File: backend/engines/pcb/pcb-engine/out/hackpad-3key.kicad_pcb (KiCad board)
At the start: 2 copper layers, 58.3 x 43 mm, 8 parts, among them SW1 ESC, SW2 2, SW3 3, U1 XIAO RP2040

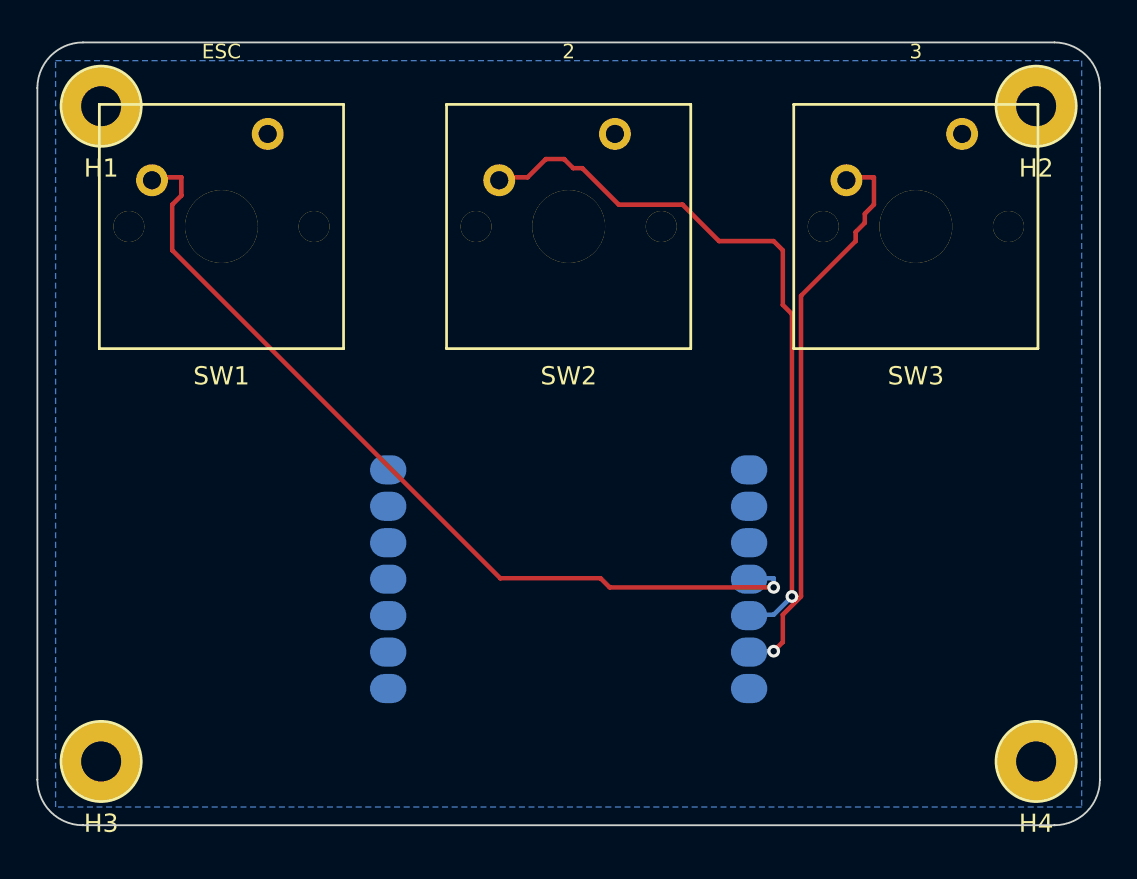
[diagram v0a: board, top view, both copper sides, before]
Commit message: case compiler: pcb result -> parametric openscad. xiao flipped 180 so usb faces the board edge. job #2 (ninepad) end to end with case artifacts. openscad-verified stls for all reference boards
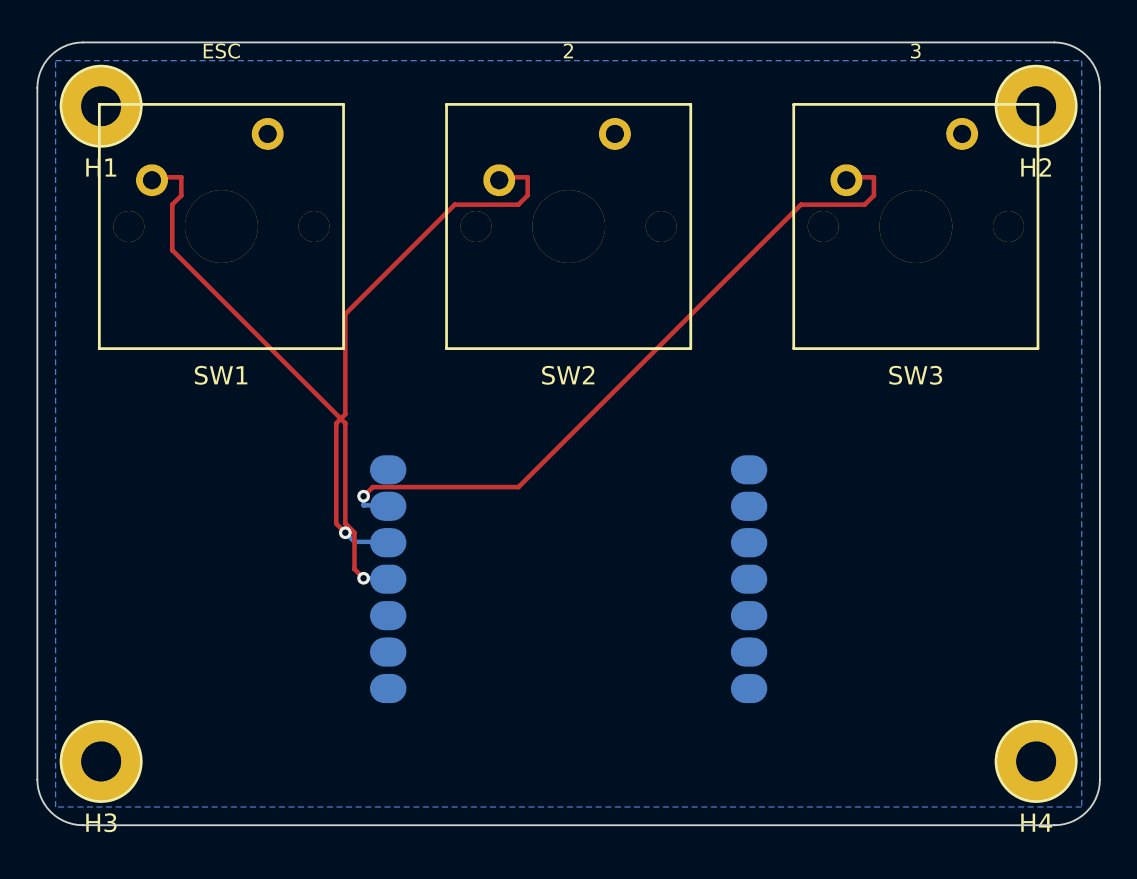
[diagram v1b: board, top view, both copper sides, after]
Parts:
- turned U1 to -180 degrees
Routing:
- net K1: track 48.4 -> 29.6 mm
- net K2: track 40.1 -> 30.3 mm
- net K3: track 31.3 -> 39.3 mm
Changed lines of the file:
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@@
   (pad "peg1" thru_hole circle (at -5.08 0) (size 1.7 1.7) (drill 1.7) (layers "*.Cu" "*.Mask") (remove_unused_layers) (keep_end_layers))
   (pad "peg2" thru_hole circle (at 5.08 0) (size 1.7 1.7) (drill 1.7) (layers "*.Cu" "*.Mask") (remove_unused_layers) (keep_end_layers)))
-(footprint "keeberia:Module_Seeed_XIAO" (layer B.Cu) (at 0 7.975000000000001)
+(footprint "keeberia:Module_Seeed_XIAO" (layer B.Cu) (at 0 7.975000000000001 -180)
   (attr smd)
   (fp_text reference "U1" (at 0 -9.95) (layer B.SilkS) (effects (font (size 1 1) (thickness 0.15))))
@@
   (fp_circle (center 0 0) (end 2.2 0) (stroke (width 0.15) (type solid)) (fill none) (layer F.SilkS))
   (pad "1" thru_hole circle (at 0 0) (size 4.4 4.4) (drill 2.2) (layers "*.Cu" "*.Mask") (remove_unused_layers) (keep_end_layers)))
+  (segment (start 15.25 -14.075) (end 16.75 -14.075) (width 0.25) (layer F.Cu) (net 5 "K3"))
+  (segment (start 16.75 -14.075) (end 16.75 -13.075) (width 0.25) (layer F.Cu) (net 5 "K3"))
+  (segment (start 16.75 -13.075) (end 16.25 -12.575) (width 0.25) (layer F.Cu) (net 5 "K3"))
+  (segment (start 16.25 -12.575) (end 12.75 -12.575) (width 0.25) (layer F.Cu) (net 5 "K3"))
+  (segment (start 12.75 -12.575) (end -2.75 2.925) (width 0.25) (layer F.Cu) (net 5 "K3"))
+  (segment (start -2.75 2.925) (end -10.75 2.925) (width 0.25) (layer F.Cu) (net 5 "K3"))
+  (segment (start -10.75 2.925) (end -11.25 3.425) (width 0.25) (layer F.Cu) (net 5 "K3"))
+  (segment (start -11.25 3.425) (end -11.25 3.925) (width 0.25) (layer B.Cu) (net 5 "K3"))
+  (segment (start -11.25 3.925) (end -9.75 3.925) (width 0.25) (layer B.Cu) (net 5 "K3"))
   (segment (start -22.75 -14.075) (end -21.25 -14.075) (width 0.25) (layer F.Cu) (net 3 "K1"))
   (segment (start -21.25 -14.075) (end -21.25 -13.075) (width 0.25) (layer F.Cu) (net 3 "K1"))
   (segment (start -21.25 -13.075) (end -21.75 -12.575) (width 0.25) (layer F.Cu) (net 3 "K1"))
   (segment (start -21.75 -12.575) (end -21.75 -10.075) (width 0.25) (layer F.Cu) (net 3 "K1"))
-  (segment (start -21.75 -10.075) (end -3.75 7.925) (width 0.25) (layer F.Cu) (net 3 "K1"))
-  (segment (start -3.75 7.925) (end 1.75 7.925) (width 0.25) (layer F.Cu) (net 3 "K1"))
-  (segment (start 1.75 7.925) (end 2.25 8.425) (width 0.25) (layer F.Cu) (net 3 "K1"))
-  (segment (start 2.25 8.425) (end 11.25 8.425) (width 0.25) (layer F.Cu) (net 3 "K1"))
-  (segment (start 11.25 8.425) (end 11.25 7.925) (width 0.25) (layer B.Cu) (net 3 "K1"))
-  (segment (start 11.25 7.925) (end 9.75 7.925) (width 0.25) (layer B.Cu) (net 3 "K1"))
+  (segment (start -21.75 -10.075) (end -12.25 -0.575) (width 0.25) (layer F.Cu) (net 3 "K1"))
+  (segment (start -12.25 -0.575) (end -12.25 4.925) (width 0.25) (layer F.Cu) (net 3 "K1"))
+  (segment (start -12.25 4.925) (end -11.75 5.425) (width 0.25) (layer F.Cu) (net 3 "K1"))
+  (segment (start -11.75 5.425) (end -11.75 7.425) (width 0.25) (layer F.Cu) (net 3 "K1"))
+  (segment (start -11.75 7.425) (end -11.25 7.925) (width 0.25) (layer F.Cu) (net 3 "K1"))
+  (segment (start -11.25 7.925) (end -9.75 7.925) (width 0.25) (layer B.Cu) (net 3 "K1"))
   (segment (start -3.75 -14.075) (end -2.25 -14.075) (width 0.25) (layer F.Cu) (net 4 "K2"))
-  (segment (start -2.25 -14.075) (end -1.25 -15.075) (width 0.25) (layer F.Cu) (net 4 "K2"))
-  (segment (start -1.25 -15.075) (end -0.25 -15.075) (width 0.25) (layer F.Cu) (net 4 "K2"))
-  (segment (start -0.25 -15.075) (end 0.25 -14.575) (width 0.25) (layer F.Cu) (net 4 "K2"))
-  (segment (start 0.25 -14.575) (end 0.75 -14.575) (width 0.25) (layer F.Cu) (net 4 "K2"))
-  (segment (start 0.75 -14.575) (end 2.75 -12.575) (width 0.25) (layer F.Cu) (net 4 "K2"))
-  (segment (start 2.75 -12.575) (end 6.25 -12.575) (width 0.25) (layer F.Cu) (net 4 "K2"))
-  (segment (start 6.25 -12.575) (end 8.25 -10.575) (width 0.25) (layer F.Cu) (net 4 "K2"))
-  (segment (start 8.25 -10.575) (end 11.25 -10.575) (width 0.25) (layer F.Cu) (net 4 "K2"))
-  (segment (start 11.25 -10.575) (end 11.75 -10.075) (width 0.25) (layer F.Cu) (net 4 "K2"))
-  (segment (start 11.75 -10.075) (end 11.75 -7.075) (width 0.25) (layer F.Cu) (net 4 "K2"))
-  (segment (start 11.75 -7.075) (end 12.25 -6.575) (width 0.25) (layer F.Cu) (net 4 "K2"))
-  (segment (start 12.25 -6.575) (end 12.25 8.925) (width 0.25) (layer F.Cu) (net 4 "K2"))
-  (segment (start 12.25 8.925) (end 11.25 9.925) (width 0.25) (layer B.Cu) (net 4 "K2"))
-  (segment (start 11.25 9.925) (end 9.75 9.925) (width 0.25) (layer B.Cu) (net 4 "K2"))
-  (segment (start 15.25 -14.075) (end 16.75 -14.075) (width 0.25) (layer F.Cu) (net 5 "K3"))
-  (segment (start 16.75 -14.075) (end 16.75 -12.575) (width 0.25) (layer F.Cu) (net 5 "K3"))
-  (segment (start 16.75 -12.575) (end 16.25 -12.075) (width 0.25) (layer F.Cu) (net 5 "K3"))
-  (segment (start 16.25 -12.075) (end 16.25 -11.575) (width 0.25) (layer F.Cu) (net 5 "K3"))
-  (segment (start 16.25 -11.575) (end 15.75 -11.075) (width 0.25) (layer F.Cu) (net 5 "K3"))
-  (segment (start 15.75 -11.075) (end 15.75 -10.575) (width 0.25) (layer F.Cu) (net 5 "K3"))
-  (segment (start 15.75 -10.575) (end 12.75 -7.575) (width 0.25) (layer F.Cu) (net 5 "K3"))
-  (segment (start 12.75 -7.575) (end 12.75 8.925) (width 0.25) (layer F.Cu) (net 5 "K3"))
-  (segment (start 12.75 8.925) (end 11.75 9.925) (width 0.25) (layer F.Cu) (net 5 "K3"))
-  (segment (start 11.75 9.925) (end 11.75 11.425) (width 0.25) (layer F.Cu) (net 5 "K3"))
-  (segment (start 11.75 11.425) (end 11.25 11.925) (width 0.25) (layer F.Cu) (net 5 "K3"))
-  (segment (start 11.25 11.925) (end 9.75 11.925) (width 0.25) (layer B.Cu) (net 5 "K3"))
-  (via (at 11.25 8.425) (size 0.7) (drill 0.35) (layers "F.Cu" "B.Cu") (net 3 "K1"))
-  (via (at 12.25 8.925) (size 0.7) (drill 0.35) (layers "F.Cu" "B.Cu") (net 4 "K2"))
-  (via (at 11.25 11.925) (size 0.7) (drill 0.35) (layers "F.Cu" "B.Cu") (net 5 "K3"))
+  (segment (start -2.25 -14.075) (end -2.25 -13.075) (width 0.25) (layer F.Cu) (net 4 "K2"))
+  (segment (start -2.25 -13.075) (end -2.75 -12.575) (width 0.25) (layer F.Cu) (net 4 "K2"))
+  (segment (start -2.75 -12.575) (end -6.25 -12.575) (width 0.25) (layer F.Cu) (net 4 "K2"))
+  (segment (start -6.25 -12.575) (end -12.25 -6.575) (width 0.25) (layer F.Cu) (net 4 "K2"))
+  (segment (start -12.25 -6.575) (end -12.25 -1.075) (width 0.25) (layer F.Cu) (net 4 "K2"))
+  (segment (start -12.25 -1.075) (end -12.75 -0.575) (width 0.25) (layer F.Cu) (net 4 "K2"))
+  (segment (start -12.75 -0.575) (end -12.75 4.925) (width 0.25) (layer F.Cu) (net 4 "K2"))
+  (segment (start -12.75 4.925) (end -12.25 5.425) (width 0.25) (layer F.Cu) (net 4 "K2"))
+  (segment (start -12.25 5.425) (end -11.75 5.925) (width 0.25) (layer B.Cu) (net 4 "K2"))
+  (segment (start -11.75 5.925) (end -9.75 5.925) (width 0.25) (layer B.Cu) (net 4 "K2"))
+  (via (at -11.25 3.425) (size 0.7) (drill 0.35) (layers "F.Cu" "B.Cu") (net 5 "K3"))
+  (via (at -11.25 7.925) (size 0.7) (drill 0.35) (layers "F.Cu" "B.Cu") (net 3 "K1"))
+  (via (at -12.25 5.425) (size 0.7) (drill 0.35) (layers "F.Cu" "B.Cu") (net 4 "K2"))
   (gr_line (start -26.65 -21.475) (end 26.65 -21.475) (stroke (width 0.1) (type solid)) (layer "Edge.Cuts"))
   (gr_arc (start 26.65 -21.475) (mid 28.4178 -20.7428) (end 29.15 -18.975) (stroke (width 0.1) (type solid)) (layer "Edge.Cuts"))
